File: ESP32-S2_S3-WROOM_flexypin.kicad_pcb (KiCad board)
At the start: 2 copper layers, 31 x 51.4 mm, 15 parts, among them J1 Conn_01x20, J2 Conn_01x14, J22 Conn_01x20, J24 USB_C_Receptacle_USB2.0_14P, J25 Conn_01x12, J26 Conn_01x14, SW1 SW_Push, SW2 SW_Push, U1 RT9080

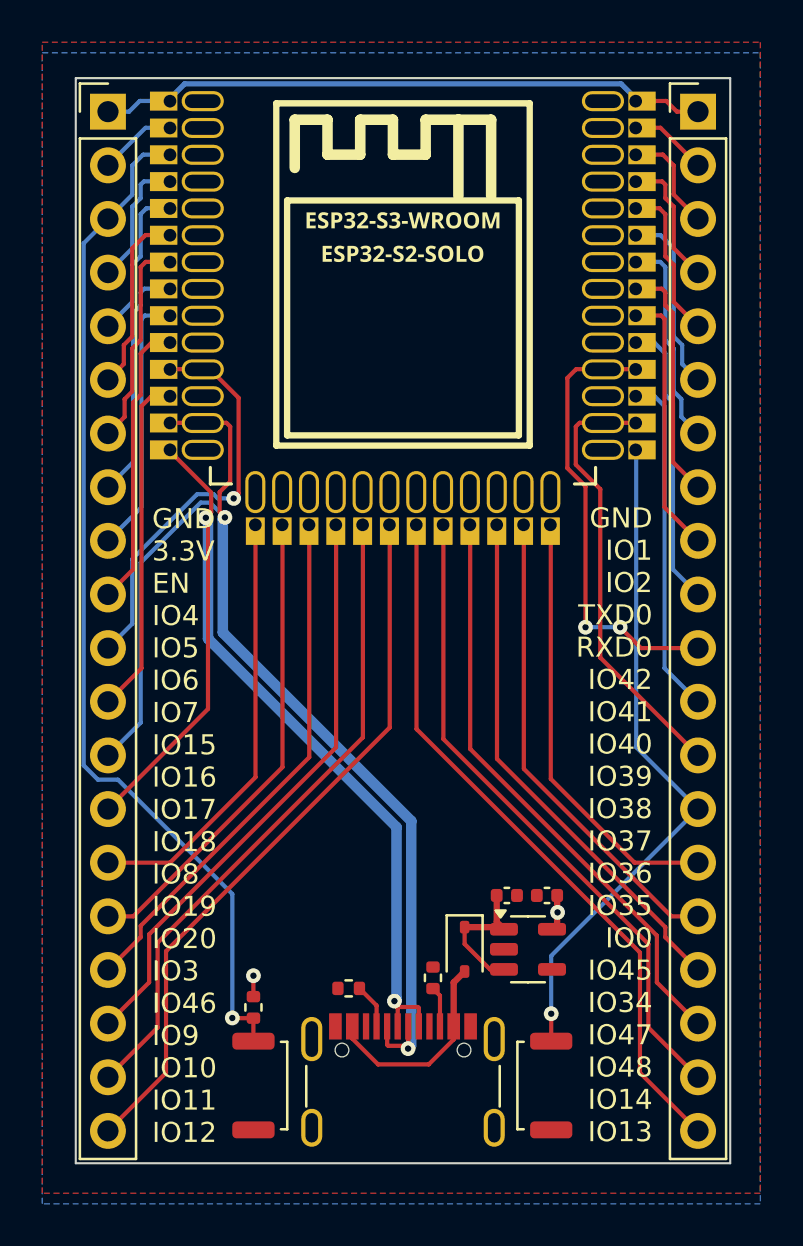
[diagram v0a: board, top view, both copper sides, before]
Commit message: added LED
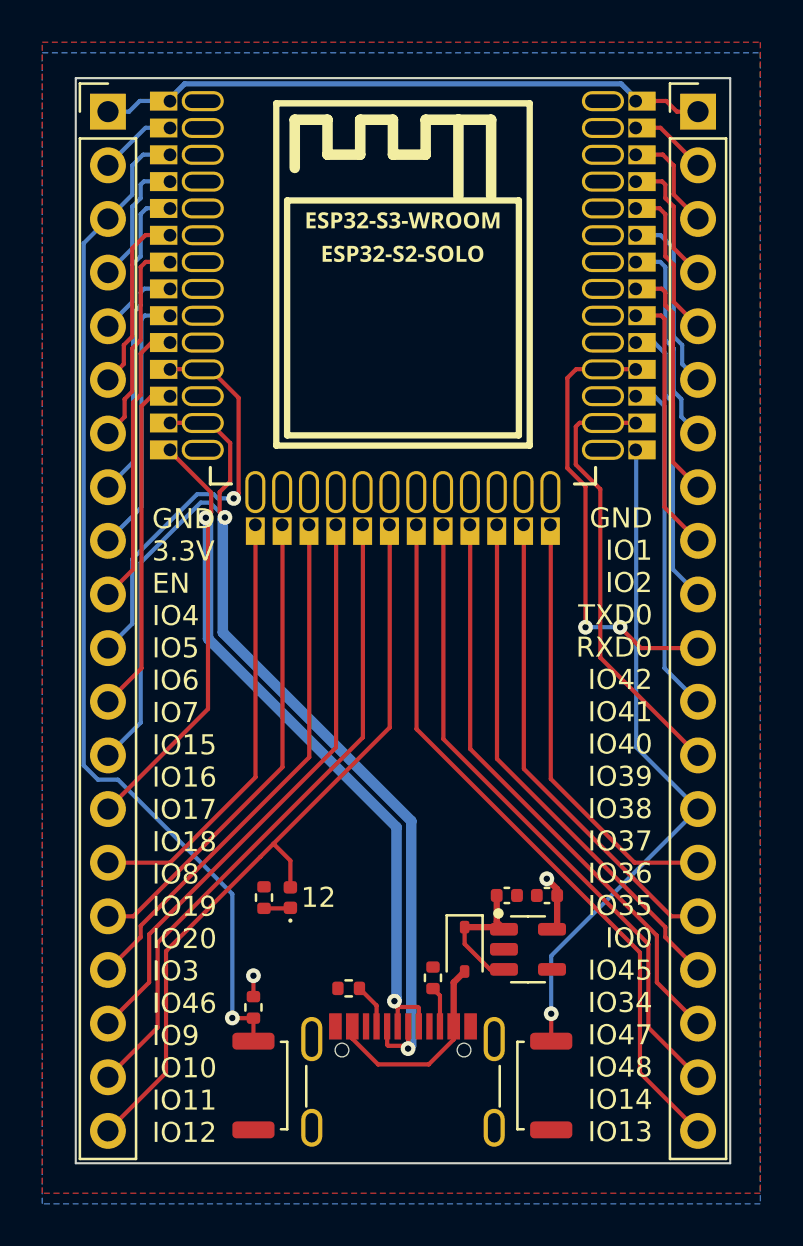
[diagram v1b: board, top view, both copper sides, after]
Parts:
- added D2: LED_Small, LED_SMD:LED_0402_1005Metric, F.Cu at (142.8, 119.0)
- added R4: 100-1kΩ, Resistor_SMD:R_0402_1005Metric, F.Cu at (141.5, 119.0)
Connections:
- net /IO12 renamed IO12
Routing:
- net IO12: track 34.2 -> 36.6 mm
- net +3.3V: track 6.37 -> 7.65 mm
- net Net-(D2-K): track 0.00 -> 1.26 mm
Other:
- board text added: "12"

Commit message: mislabeling
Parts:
- moved R1 0.70 mm to (140.9, 123.5)
- moved SW1 0.70 mm to (140.9, 127.2)
- moved SW2 0.70 mm to (155.2, 127.2)
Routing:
- net GND: track 28.9 -> 6.28 mm
- net EN: track 48.9 -> 48.1 mm
- net IO0: track 32.1 -> 31.4 mm
- net IO19: track 54.3 -> 54.9 mm
- net IO20: track 50.0 -> 50.5 mm
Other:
- board size 31 x 51.4 mm -> 31 x 51.5 mm
- board text added: "BT"
- board text added: "GND IO1 IO2 TXD0 RXD0 IO42 IO41 IO40 IO39 IO38 IO37 IO36 IO35 IO0 IO45 IO34 IO47_{(S3)}/ IO33_{(S2)} IO48_{(S3)}/ IO34_{(S2)} IO14 IO13"
- board text added: "IO12"
- board text added: "RST"
- board text removed: "12"
- board text removed: "GND IO1 IO2 TXD0 RXD0 IO42 IO41 IO40 IO39 IO38 IO37 IO36 IO35 IO0 IO45 IO34 IO47_{(S3)}/IO33_{(S2)} IO48_{(S3)}/IO34_{(S2)} IO14 IO13"
